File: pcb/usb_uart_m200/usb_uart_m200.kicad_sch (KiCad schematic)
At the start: 19 parts, among them J1 Conn_01x02_Socket, J2 Conn_01x08_Pin, J3 Conn_01x05_Pin, J4 USB_A, J5 Conn_01x01_Socket, P1 USB_C_Plug_USB2.0, P2 USB_C_Plug_USB2.0, U1 CY7C65213-28PVXI, U2 TC1015-xCT, U3 TPD2EUSB30

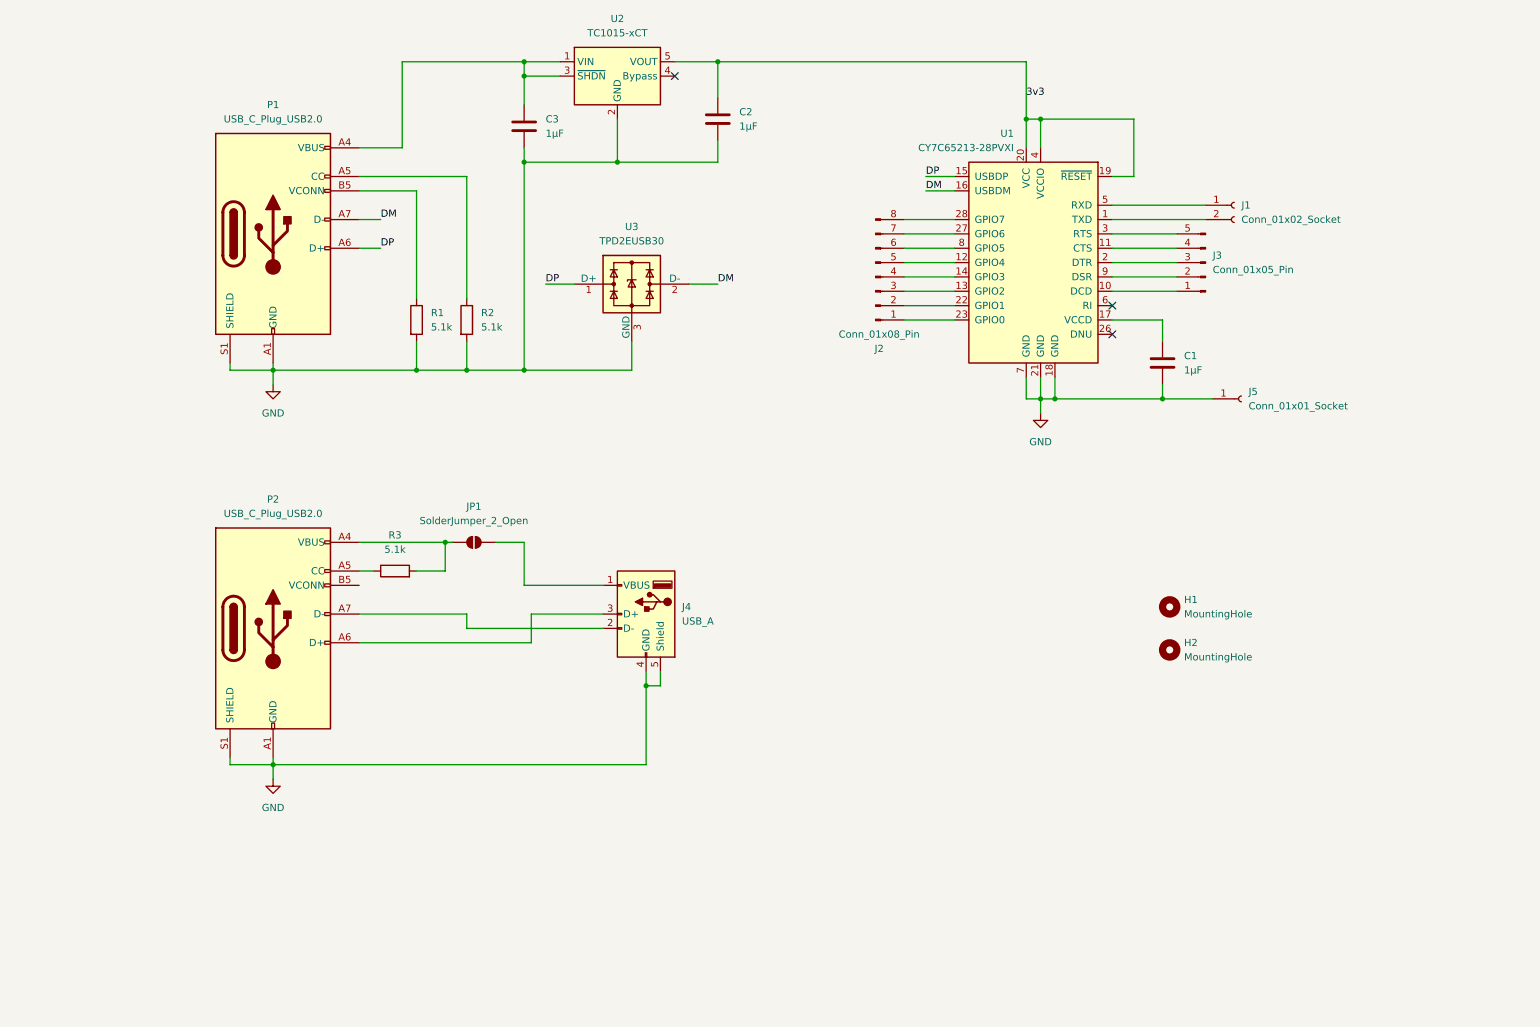
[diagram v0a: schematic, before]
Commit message: First draft of the MCU programmer / linux serial console.
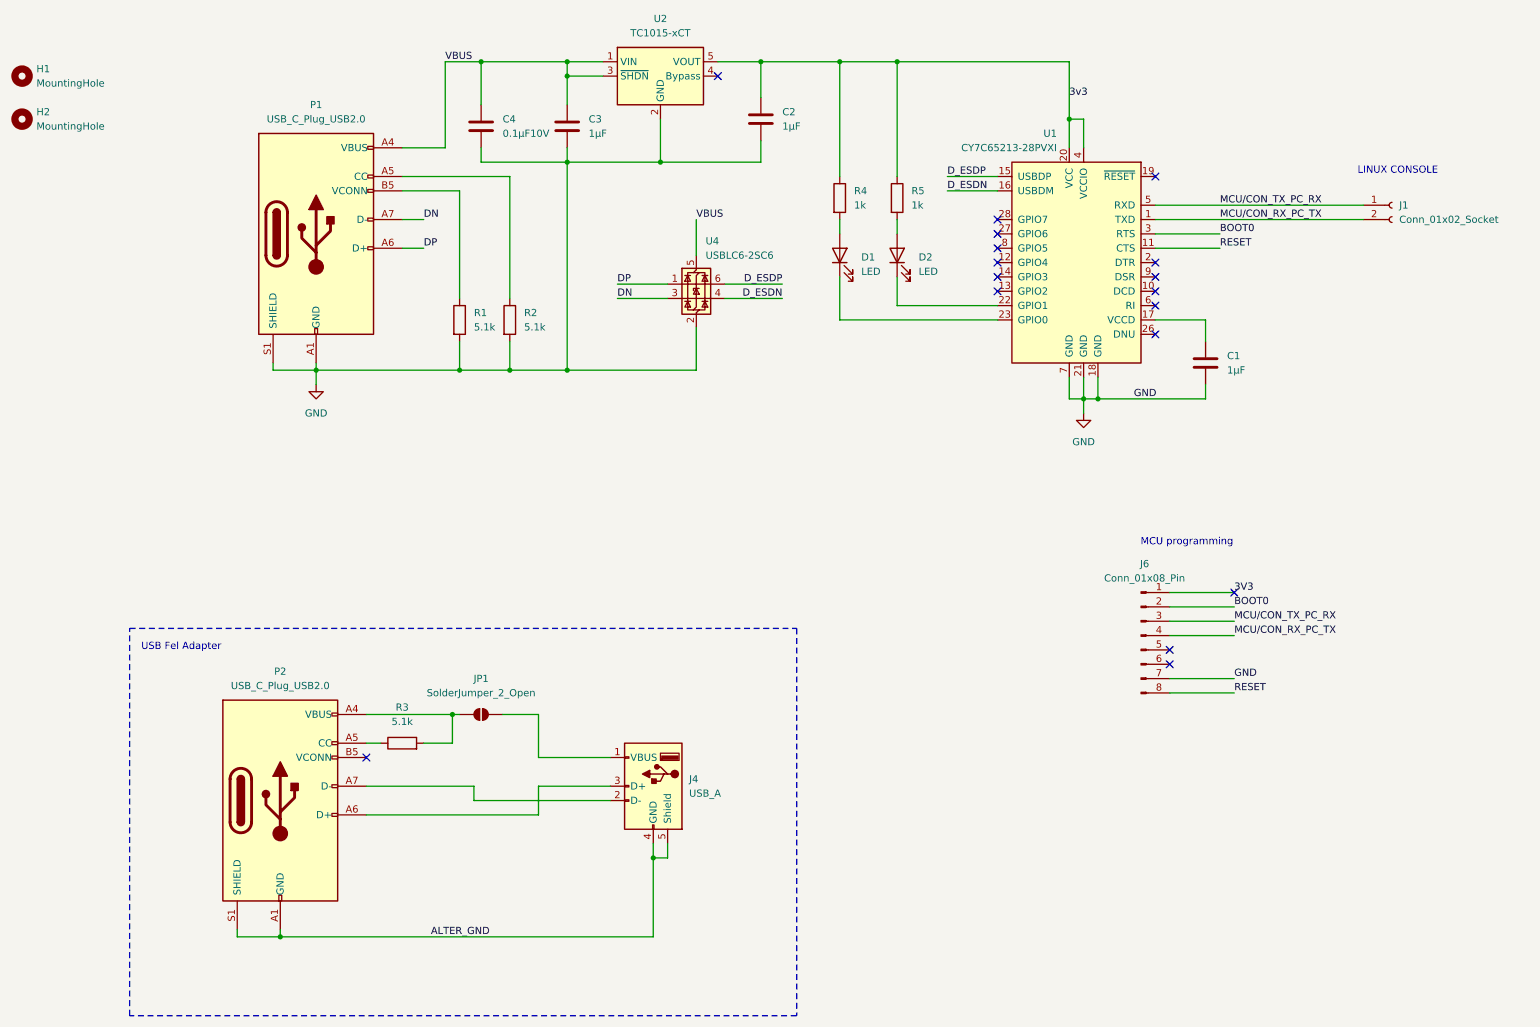
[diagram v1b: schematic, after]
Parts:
- removed J2: Conn_01x08_Pin, symbol Connector:Conn_01x08_Pin
- removed J3: Conn_01x05_Pin, symbol Connector:Conn_01x05_Pin
- removed J5: Conn_01x01_Socket, symbol Connector:Conn_01x01_Socket
- removed U3: TPD2EUSB30, Package_TO_SOT_SMD:Texas_DRT-3, symbol Power_Protection:TPD2EUSB30
- added C4: 0.1µF10V, Capacitor_SMD:C_0805_2012Metric, symbol Device:C
- added D1, D2: LED, LED_SMD:LED_0805_2012Metric_Pad1.15x1.40mm_HandSolder, symbol Device:LED
- added J6: Conn_01x08_Pin, Connector_PinHeader_2.54mm:PinHeader_1x08_P2.54mm_Vertical, symbol Connector:Conn_01x08_Pin
- added R4, R5: 1k, Resistor_SMD:R_0805_2012Metric, symbol Device:R
- added U4: USBLC6-2SC6, Package_TO_SOT_SMD:SOT-23-6, symbol Power_Protection:USBLC6-2SC6
- C1, C2, C3: footprint (none) -> Capacitor_SMD:C_0805_2012Metric
- H1, H2: footprint (none) -> MountingHole:MountingHole_3.2mm_M3_DIN965_Pad_TopBottom
- J1: footprint (none) -> Connector_Molex:Molex_PicoBlade_53047-0210_1x02_P1.25mm_Vertical
- J4: footprint (none) -> Connector_USB:USB_A_Molex_48037-2200_Horizontal
- JP1: footprint (none) -> Jumper:SolderJumper-2_P1.3mm_Open_TrianglePad1.0x1.5mm
- P1, P2: footprint (none) -> Connector_USB:USB_C_Receptacle_G-Switch_GT-USB-7010ASV
- R1, R2, R3: footprint (none) -> Resistor_SMD:R_0805_2012Metric
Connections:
- net 3v3: now also R4.1, R5.1; no longer U1.19 (~{RESET})
- net DP: now also U4.1 (I/O1); no longer U1.15 (USBDP)
- net GND: now also C4.2, J6.7 (Pin_7), U4.2 (GND); no longer J4.4 (GND), J4.5 (Shield), P2.A1 (GND), P2.A12 (GND), P2.B1 (GND), P2.B12 (GND), P2.S1 (SHIELD)
- net VBUS: now reaches C3.1, P1.A4 (VBUS), P1.A9 (VBUS), P1.B4 (VBUS), P1.B9 (VBUS), U2.1 (VIN), U2.3 (~{SHDN})
- net VBUS: now also C4.1, U4.5 (VBUS)
- net MCU/CON_TX_PC_RX: now reaches J1.1 (Pin_1), U1.5 (RXD)
- net MCU/CON_TX_PC_RX: now also J6.3 (Pin_3)
- net MCU/CON_RX_PC_TX: now reaches J1.2 (Pin_2), U1.1 (TXD)
- net MCU/CON_RX_PC_TX: now also J6.4 (Pin_4)
- net RESET: now reaches U1.11 (CTS)
- net RESET: now also J6.8 (Pin_8)
- net BOOT0: now reaches U1.3 (RTS)
- net BOOT0: now also J6.2 (Pin_2)
- net at U1.23 (GPIO0): now also D1.1 (K)
- net at U1.22 (GPIO1): now also D2.1 (K)
- net DM renamed DN
- net DN: now also U4.3 (I/O2); no longer U1.16 (USBDM)
- new net: D1.2 (A), R4.2
- new net: D2.2 (A), R5.2
- new net 3V3: J6.1 (Pin_1)
- new net ALTER_GND: J4.4 (GND), J4.5 (Shield), P2.A1 (GND), P2.A12 (GND), P2.B1 (GND), P2.B12 (GND), P2.S1 (SHIELD)
- new net D_ESDN: U1.16 (USBDM), U4.4 (I/O2)
- new net D_ESDP: U1.15 (USBDP), U4.6 (I/O1)
- no-connect marks 3 -> 17
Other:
- note added: "LINUX CONSOLE"
- note added: "MCU programming"
- note added: "USB Fel Adapter"
- moved on the sheet: C1, C2, C3, H1, H2, J1, J4, JP1, P1, P2, R1, R2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

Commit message: Routing
Separated the uart from the FEL adapter board.
Adds a led wire connector for the ground pin.
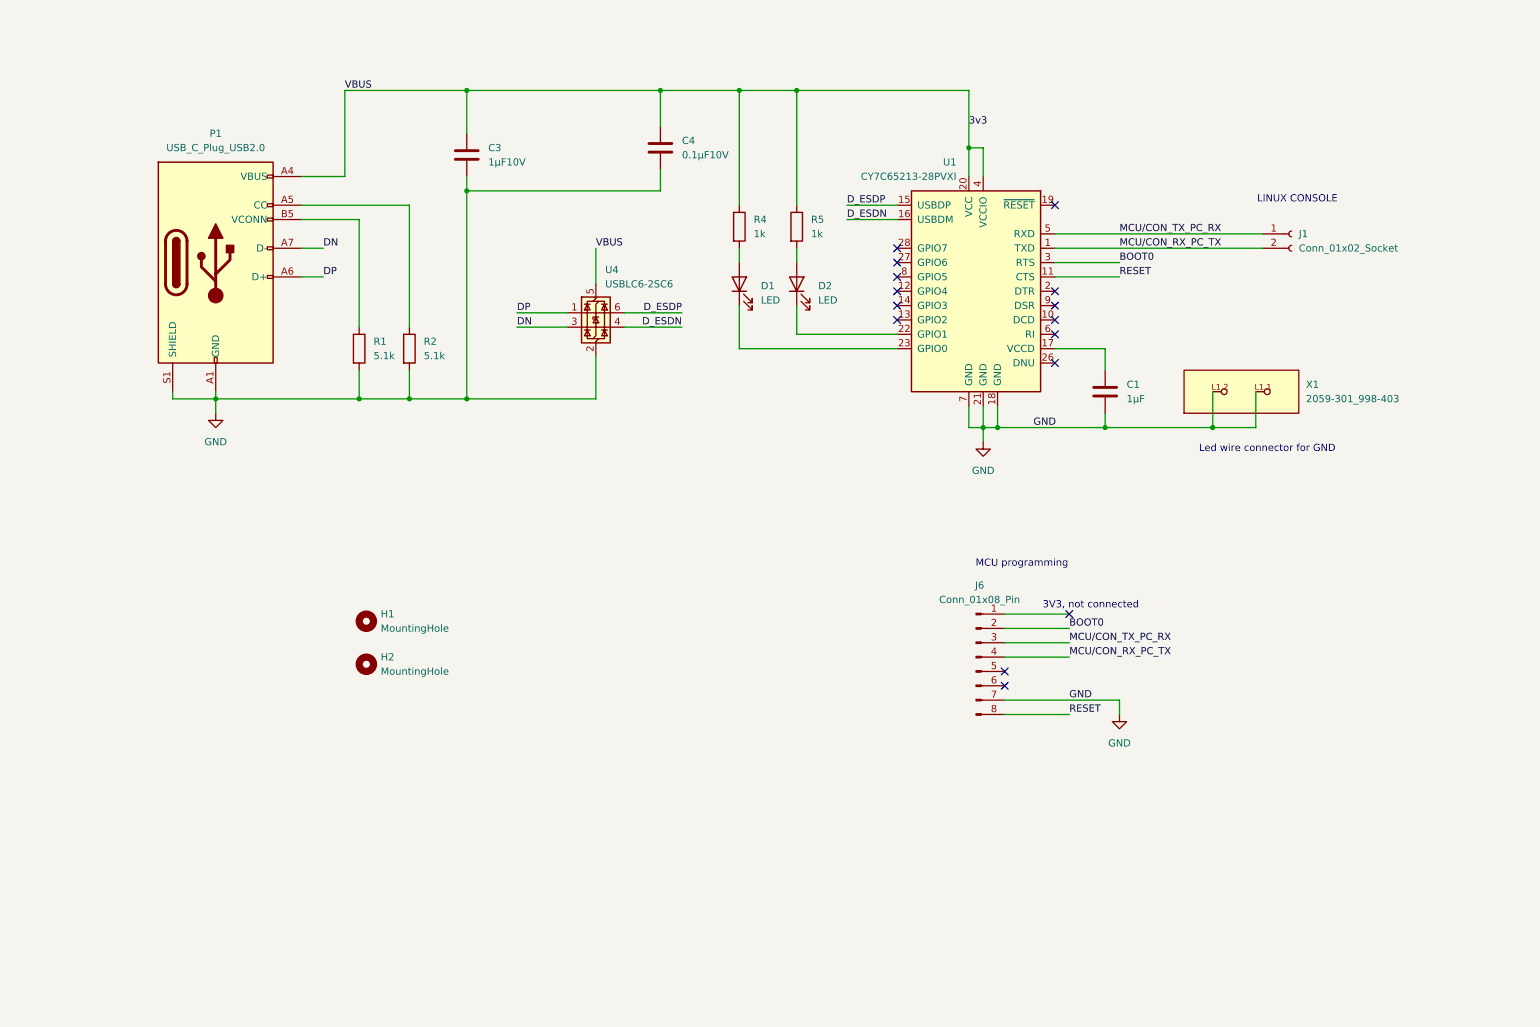
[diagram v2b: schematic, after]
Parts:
- removed C2: 1µF, Capacitor_SMD:C_0805_2012Metric, symbol Device:C
- removed J4: USB_A, Connector_USB:USB_A_Molex_48037-2200_Horizontal, symbol Connector:USB_A
- removed JP1: SolderJumper_2_Open, Jumper:SolderJumper-2_P1.3mm_Open_TrianglePad1.0x1.5mm, symbol Jumper:SolderJumper_2_Open
- removed P2: USB_C_Plug_USB2.0, Connector_USB:USB_C_Receptacle_G-Switch_GT-USB-7010ASV, symbol Connector:USB_C_Plug_USB2.0
- removed R3: 5.1k, Resistor_SMD:R_0805_2012Metric, symbol Device:R
- removed U2: TC1015-xCT, Package_TO_SOT_SMD:SOT-23-5, symbol Regulator_Linear:TC1015-xCT
- added X1: 2059-301_998-403, 2059-301_998-403:P-2059-301_998-403, symbol 2059-301_998-403:2059-301_998-403
- C3: value 1µF -> 1µF10V
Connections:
- net VBUS is gone; now on net 3v3: C3.1, C4.1, P1.A4 (VBUS), P1.A9 (VBUS), P1.B4 (VBUS), P1.B9 (VBUS), U4.5 (VBUS)
- net GND: now also X1.L1.1, X1.L1.2
- net 3V3: no longer names the net of J6.1 (Pin_1)
- no-connect marks 17 -> 15
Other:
- note added: "3V3, not connected"
- note added: "Led wire connector for GND"
- note removed: "USB Fel Adapter"
- moved on the sheet: C1, C3, C4, D1, D2, H1, H2, J1, J6, P1, R1, R2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

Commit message: Fix the board: add a regulator and farnelle references. Add a pull up on boot0
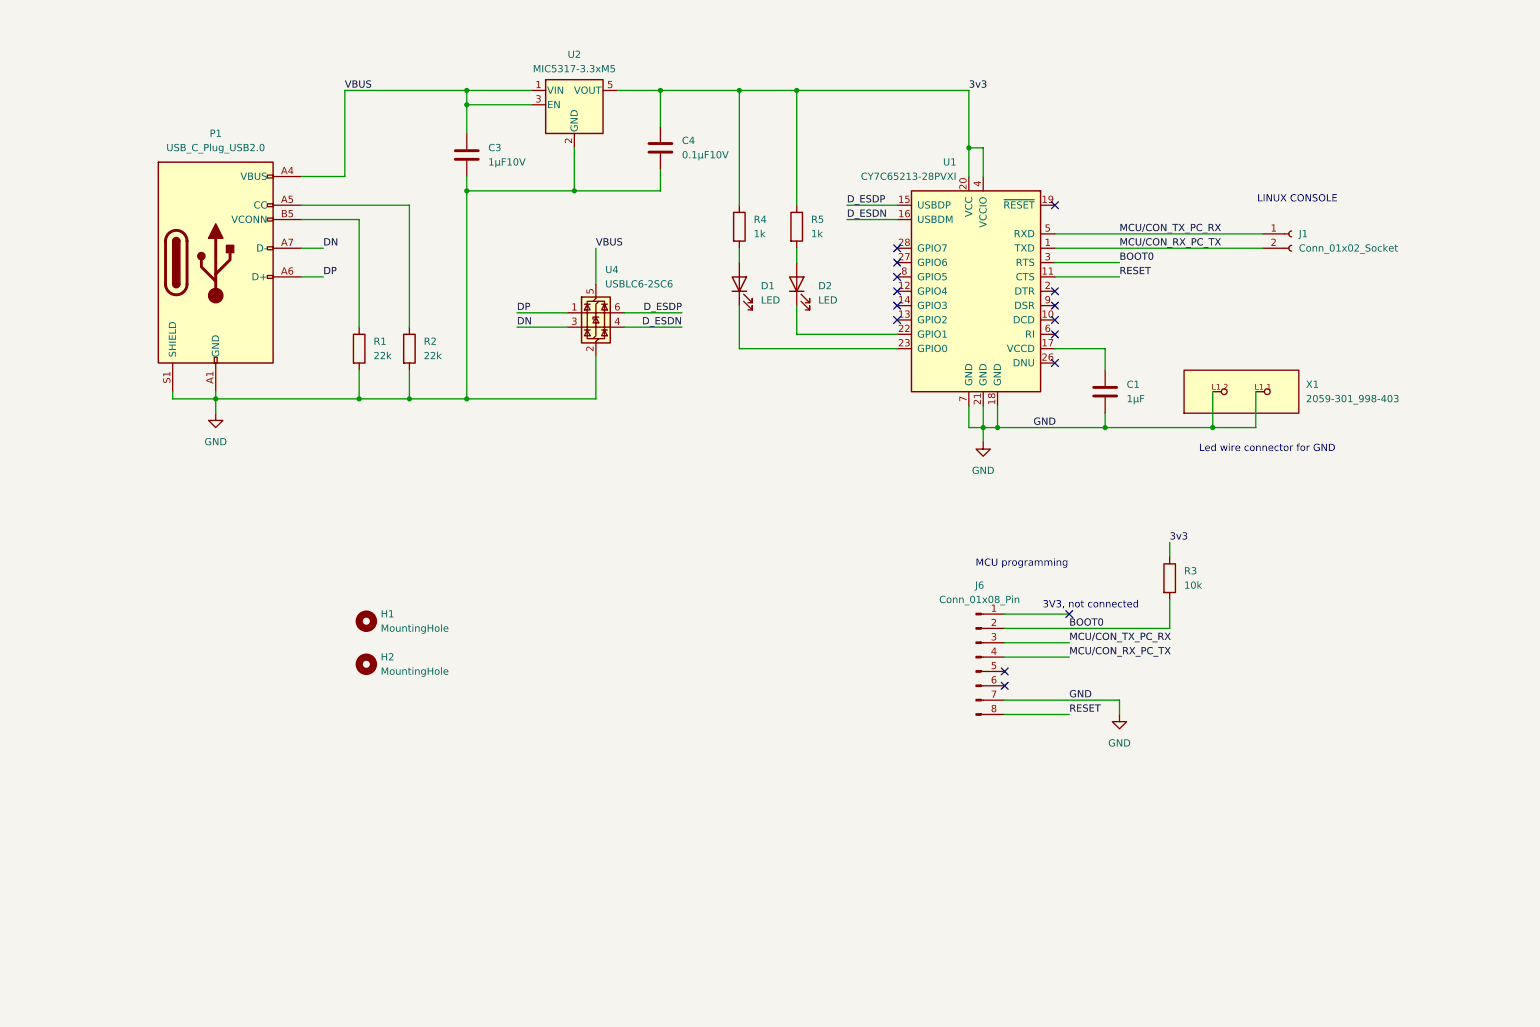
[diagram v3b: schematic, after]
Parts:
- added R3: 10k, Resistor_SMD:R_0805_2012Metric, symbol Device:R
- added U2: MIC5317-3.3xM5, Package_TO_SOT_SMD:SOT-23-5, symbol Regulator_Linear:MIC5317-3.3xM5
- J1: farnell (none) -> 9733051
- J6: farnell (none) -> 3729173
- P1: farnell (none) -> 3777659
- R1, R2: value 5.1k -> 22k; farnell (none) -> 2073691
- U1: farnell (none) -> 2772892
- U4: farnell (none) -> 1269406
- X1: farnell (none) -> 2452830
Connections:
- net 3v3: now also R3.1, U2.5 (VOUT); no longer C3.1, P1.A4 (VBUS), P1.A9 (VBUS), P1.B4 (VBUS), P1.B9 (VBUS), U4.5 (VBUS)
- net BOOT0: now also R3.2
- net GND: now also U2.2 (GND)
- new net VBUS: C3.1, P1.A4 (VBUS), P1.A9 (VBUS), P1.B4 (VBUS), P1.B9 (VBUS), U2.1 (VIN), U2.3 (EN), U4.5 (VBUS)

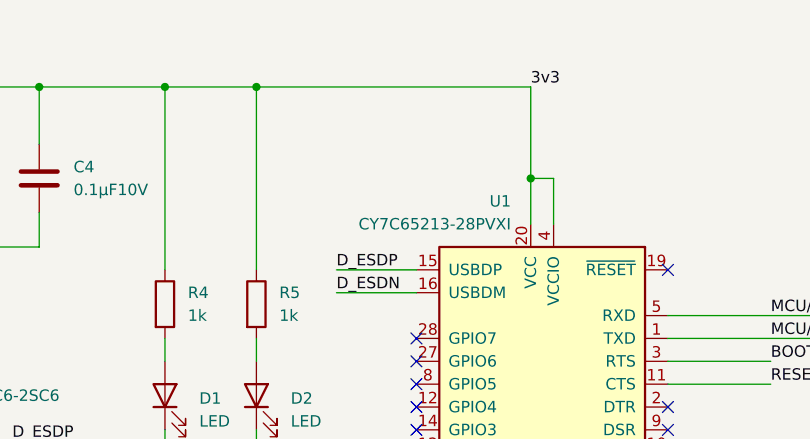
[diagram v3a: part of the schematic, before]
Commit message: Fix on the usb uart power, it uses vbus.
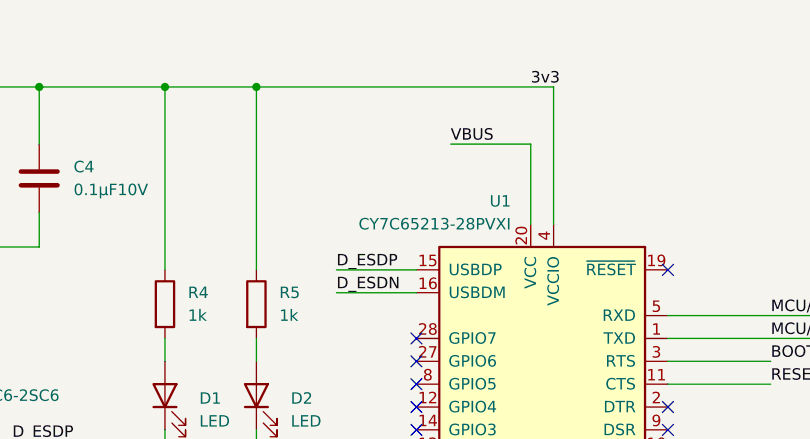
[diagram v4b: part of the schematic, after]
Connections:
- net 3v3: no longer U1.20 (VCC)
- net VBUS: now also U1.20 (VCC)
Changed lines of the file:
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@@
-	)
-	(junction
-		(at 187.96 39.37)
-		(diameter 0)
-		(color 0 0 0 0)
 	)
 	(junction
@@
 	(wire
 		(pts
-			(xy 187.96 29.21) (xy 187.96 39.37)
-		)
-		(stroke
-			(width 0)
-			(type default)
-		)
-	)
-	(wire
-		(pts
 			(xy 54.61 83.82) (xy 54.61 86.36)
 		)
@@
 	(wire
 		(pts
-			(xy 187.96 39.37) (xy 190.5 39.37)
-		)
-		(stroke
-			(width 0)
-			(type default)
-		)
-	)
-	(wire
-		(pts
 			(xy 203.2 62.23) (xy 214.63 62.23)
 		)
@@
 	(wire
 		(pts
-			(xy 187.96 39.37) (xy 187.96 44.45)
-		)
-		(stroke
-			(width 0)
-			(type default)
-		)
-	)
-	(wire
-		(pts
 			(xy 80.01 71.12) (xy 80.01 52.07)
 		)
@@
 	(wire
 		(pts
-			(xy 190.5 44.45) (xy 190.5 39.37)
-		)
-		(stroke
-			(width 0)
-			(type default)
-		)
-	)
-	(wire
-		(pts
-			(xy 157.48 29.21) (xy 187.96 29.21)
+			(xy 157.48 29.21) (xy 190.5 29.21)
 		)
 		(stroke
@@
 	(wire
 		(pts
+			(xy 190.5 29.21) (xy 190.5 44.45)
+		)
+		(stroke
+			(width 0)
+			(type default)
+		)
+	)
+	(wire
+		(pts
 			(xy 99.06 83.82) (xy 121.92 83.82)
 		)
@@
 	(wire
 		(pts
+			(xy 187.96 44.45) (xy 187.96 35.56)
+		)
+		(stroke
+			(width 0)
+			(type default)
+		)
+	)
+	(wire
+		(pts
 			(xy 99.06 29.21) (xy 110.49 29.21)
 		)
@@
 		(pts
 			(xy 107.95 71.12) (xy 116.84 71.12)
+		)
+		(stroke
+			(width 0)
+			(type default)
+		)
+	)
+	(wire
+		(pts
+			(xy 179.07 35.56) (xy 187.96 35.56)
 		)
 		(stroke
@@
 		(effects
 			(font
+				(size 1.27 1.27)
+			)
+			(justify left bottom)
+		)
+	)
+	(label "VBUS"
+		(at 179.07 35.56 0)
+		(effects
+			(font
